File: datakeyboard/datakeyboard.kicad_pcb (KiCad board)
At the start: 2 copper layers, 57.3 x 41.2 mm, 43 parts, among them Q1 BSS83P, Q2 BSS83P, Q3 BSS83P, SW1 SW_Push, SW2 SW_Push, SW3 SW_Push, SW4 SW_Push, SW5 SW_Push, SW6 SW_Push, U1 PIC24FJ128GB204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

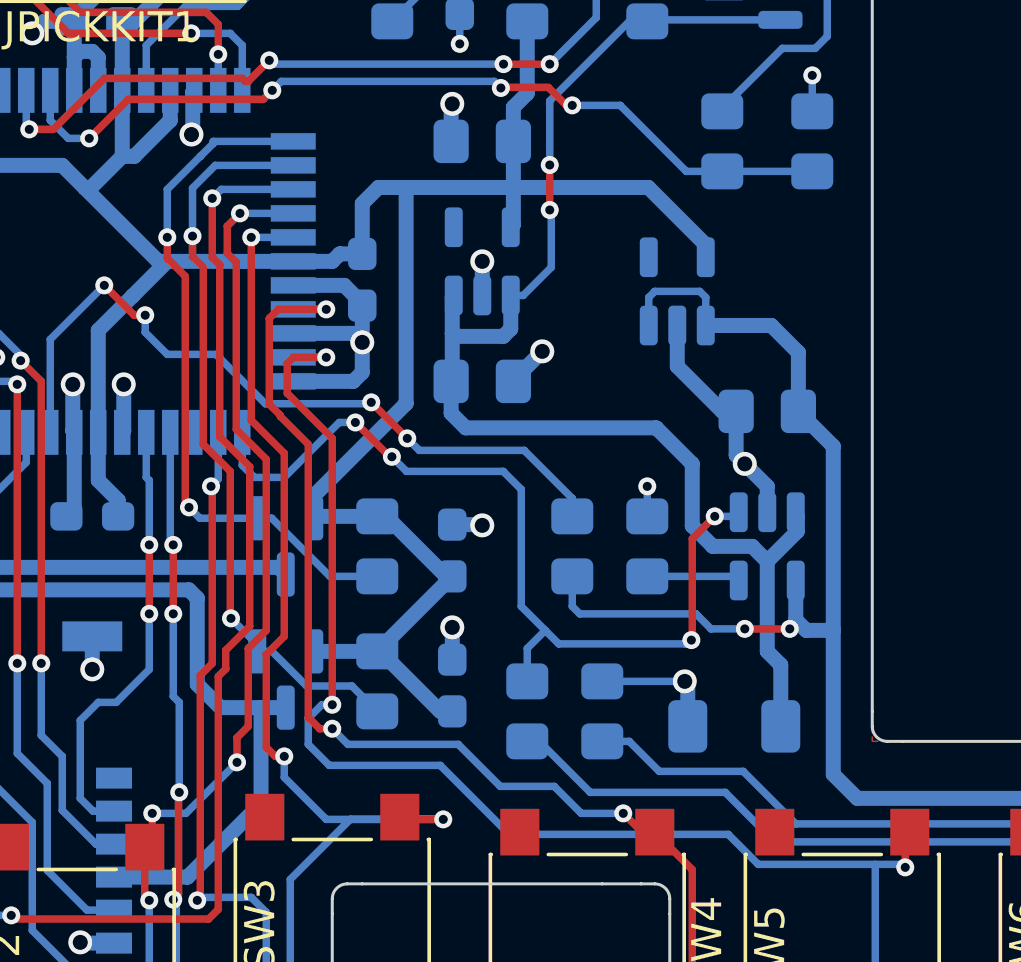
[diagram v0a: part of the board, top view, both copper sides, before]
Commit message: Control charging by microcontroller
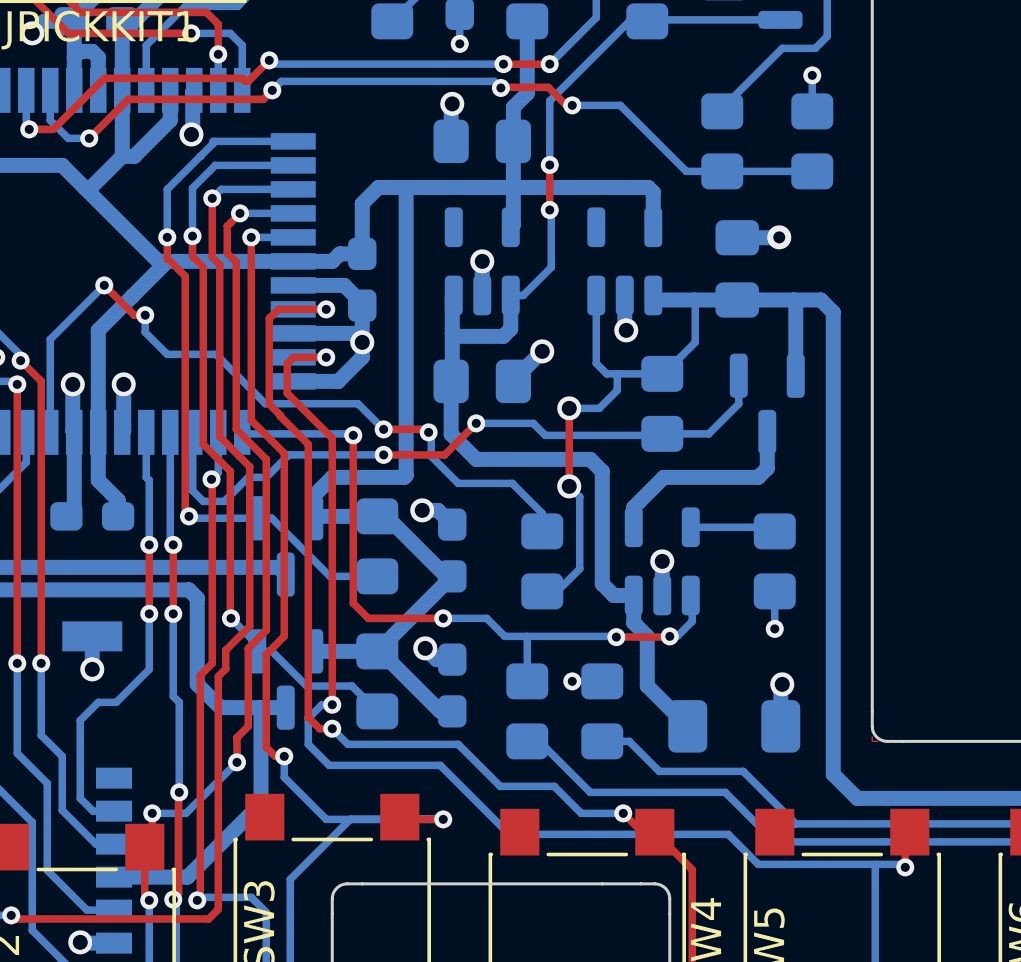
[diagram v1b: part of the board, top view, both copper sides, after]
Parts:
- added Q4: BSS83P, Package_TO_SOT_SMD:SOT-23, B.Cu at (136.5, 121.8)
- added R12: 10k, Resistor_SMD:R_0805_2012Metric_Pad1.20x1.40mm_HandSolder, B.Cu at (133.0, 121.8)
- moved C4 4.85 mm to (135.5, 117.2), turned to 90 degrees
- moved R9 4.28 mm to (136.8, 127.0), turned to 90 degrees
- moved U2 3.54 mm to (133.0, 127.0), turned to 90 degrees
- moved U4 2.02 mm to (131.8, 117.0)
- moved R1 1.12 mm to (129.0, 127.0)
- turned JBAT1 to 0 degrees
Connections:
- U1 pad 36: unconnected-(U1-Pad36) -> /CHRG_PWR
- U2 pad 4: /VUSB -> Net-(U2-Pad4)
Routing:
- net /CHRG_PWR: track 0.00 -> 22.9 mm, vias 0 -> 2
- net /VUSB: track 66.4 -> 73.8 mm
- net Net-(U2-Pad4): track 0.00 -> 6.86 mm
- net /CHRG: track 29.9 -> 23.7 mm
- net GND: track 66.1 -> 60.3 mm, vias 25 -> 28
- net /VBAT: track 44.8 -> 39.6 mm

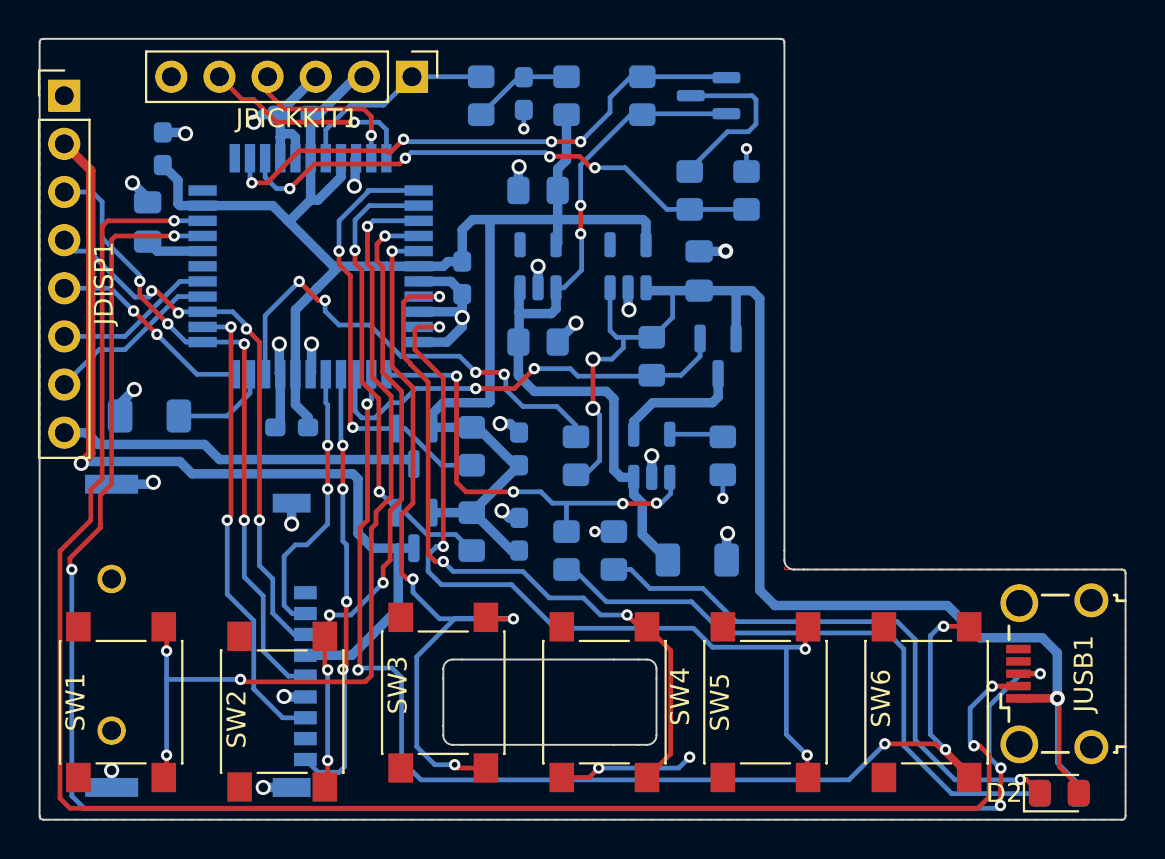
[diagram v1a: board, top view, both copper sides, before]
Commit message: Resize solder pads
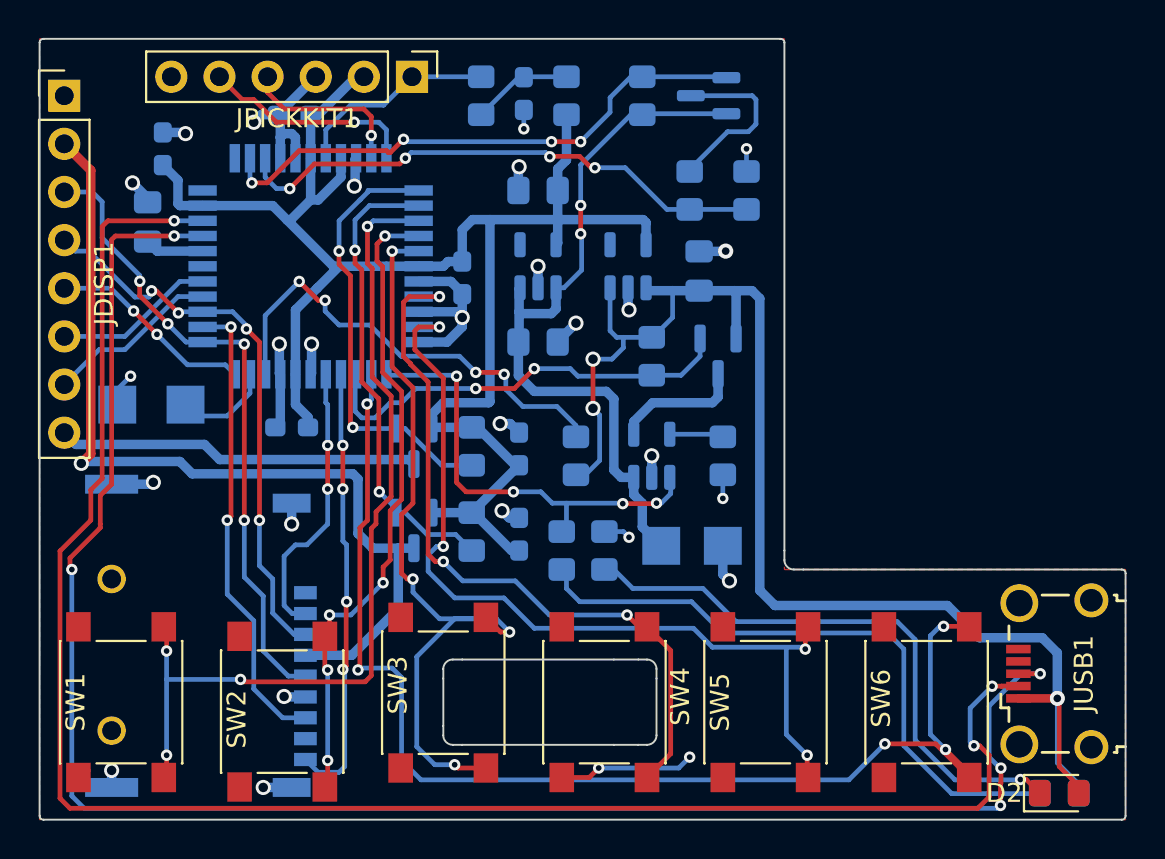
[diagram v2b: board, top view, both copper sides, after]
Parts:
- added JBAT2: Conn_01x01, TestPoint:TestPoint_Pad_2.0x2.0mm, B.Cu at (136.8, 131.8)
- added JCASE2: Conn_01x01, TestPoint:TestPoint_Pad_2.0x2.0mm, B.Cu at (104.8, 124.3)
- JBAT1, JCASE1: value Conn_01x02 -> Conn_01x01; footprint Resistor_SMD:R_1206_3216Metric_Pad1.30x1.75mm_HandSolder -> TestPoint:TestPoint_Pad_2.0x2.0mm
- moved JBAT1 2.04 mm to (133.5, 131.8)
- moved JCASE1 1.99 mm to (108.4, 124.3)
- moved R3 0.50 mm to (130.5, 132.0)
- moved R2 0.25 mm to (128.2, 132.0)
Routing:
- net GND: track 60.3 -> 61.4 mm
- net /VBAT: track 39.6 -> 38.7 mm
- net /BTN3: track 42.7 -> 42.0 mm
- net Net-(D1-Pad1): track 33.3 -> 33.9 mm

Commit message: Redesign power supply to bypass charger when running from USB
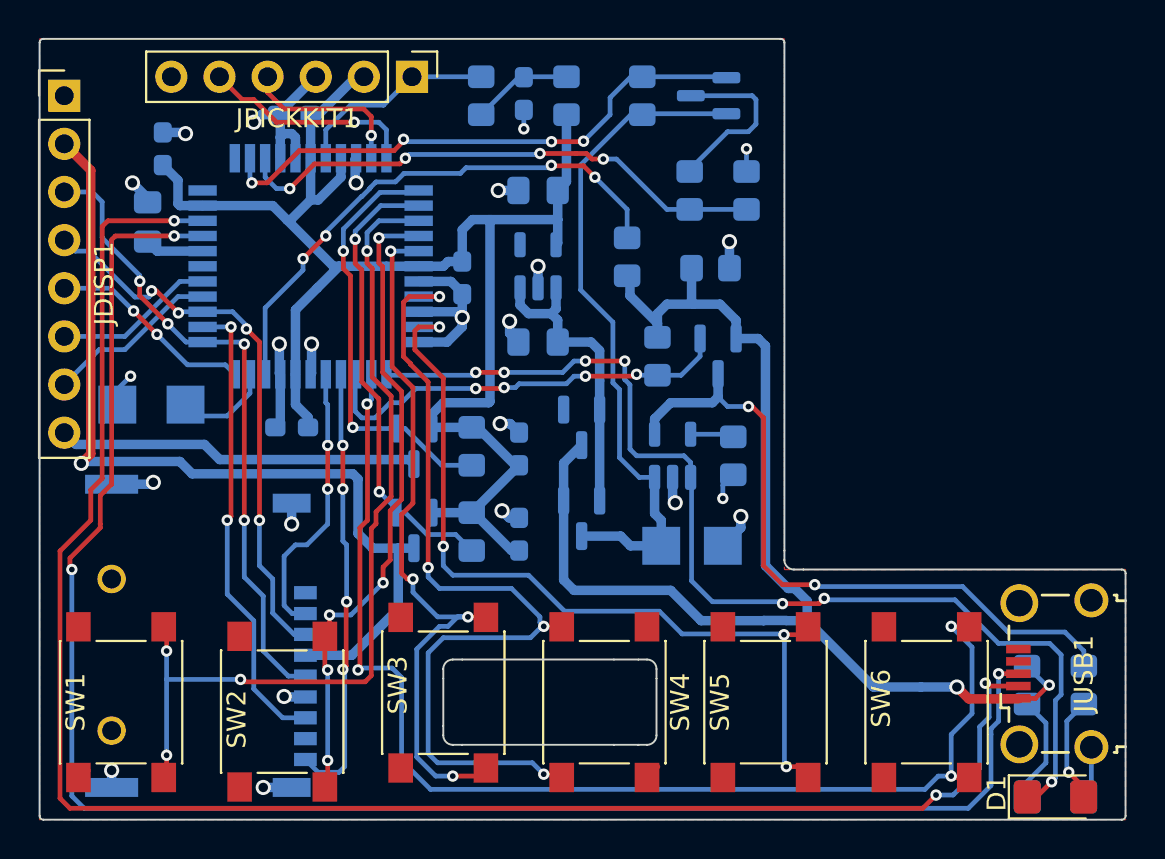
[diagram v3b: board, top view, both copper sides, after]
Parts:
- removed C4: 10uF, Capacitor_SMD:C_0805_2012Metric_Pad1.18x1.45mm_HandSolder
- removed U4: STLQ015M33R, Package_TO_SOT_SMD:SOT-23-5
- added D3: BAS40-06, Package_TO_SOT_SMD:SOT-23, B.Cu at (129.3, 125.5)
- added Q5: BSS83P, Package_TO_SOT_SMD:SOT-23, B.Cu at (129.3, 130.3)
- added R13: 10k, Resistor_SMD:R_0805_2012Metric_Pad1.20x1.40mm_HandSolder, B.Cu at (136.1, 117.1)
- D1: footprint LED_SMD:LED_0805_2012Metric_Pad1.15x1.40mm_HandSolder -> Diode_SMD:D_1206_3216Metric_Pad1.42x1.75mm_HandSolder; moved to F.Cu
- D2: footprint LED_SMD:LED_0805_2012Metric_Pad1.15x1.40mm_HandSolder -> Diode_SMD:D_1206_3216Metric_Pad1.42x1.75mm_HandSolder; moved to B.Cu
- moved R2 28.5 mm to (155.8, 139.1)
- moved R3 23.4 mm to (152.8, 139.1), turned to -90 degrees
- moved R1 10.8 mm to (131.7, 116.5)
- moved U2 1.10 mm to (134.1, 127.0)
- moved R9 0.55 mm to (137.3, 127.0)
- moved R12 0.30 mm to (133.3, 121.8), turned to 90 degrees
- moved D1 0.28 mm to (154.3, 145.0)
- moved D2 0.28 mm to (154.3, 145.0), turned to 180 degrees
- turned C1 to 180 degrees
- turned SW4 to -90 degrees
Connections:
- C1 pad 1: /VBAT -> Net-(C1-Pad1)
- D1 pad 1: Net-(D1-Pad1) -> /CHRG
- D1 pad 2: /VUSB -> Net-(D1-Pad2)
- D2 pad 1: Net-(D2-Pad1) -> GND
- D2 pad 2: /VUSB -> Net-(R3-Pad2)
- Q4 pad 3: Net-(Q4-Pad3) -> Net-(U2-Pad4)
- R12 pad 1: /VUSB -> /CHRG_PWR
- R12 pad 2: /CHRG_PWR -> /VUSB
- R2 pad 1: Net-(D1-Pad1) -> Net-(D1-Pad2)
- R2 pad 2: /CHRG -> Net-(U2-Pad4)
- R3 pad 1: Net-(D2-Pad1) -> /VUSB
- R3 pad 2: GND -> Net-(R3-Pad2)
- U2 pad 4: Net-(Q4-Pad3) -> Net-(U2-Pad4)
- U3 pad 1: /VBAT -> Net-(C1-Pad1)
- U3 pad 3: /VBAT -> Net-(C1-Pad1)
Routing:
- net Net-(U2-Pad4): track 0.00 -> 36.1 mm, vias 0 -> 2
- net Net-(D1-Pad1): track 33.9 -> 0.00 mm
- net /CHRG: track 23.7 -> 57.3 mm, vias 4 -> 7
- net Net-(D2-Pad1): track 30.5 -> 0.00 mm, vias 1 -> 0
- net Net-(C1-Pad1): track 0.00 -> 16.2 mm
- net /BTN4: track 39.1 -> 46.0 mm, vias 3 -> 4
- net Net-(Q4-Pad3): track 6.86 -> 0.00 mm
- net GND: track 61.4 -> 55.1 mm, vias 28 -> 24
- net /VUSB: track 73.8 -> 67.7 mm, vias 3 -> 2
- net +3V0: track 89.5 -> 83.6 mm
- net Net-(R3-Pad2): track 0.00 -> 5.72 mm
- net Net-(D1-Pad2): track 0.00 -> 5.64 mm, vias 0 -> 1
- net Net-(R1-Pad1): track 24.7 -> 28.7 mm
- net /BTN3: track 42.0 -> 38.4 mm
- net /VBAT: track 38.7 -> 35.6 mm, vias 2 -> 0
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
